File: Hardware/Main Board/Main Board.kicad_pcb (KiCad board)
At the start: 4 copper layers, 71 x 57.5 mm, 85 parts, among them J1 Micro_SD_Card_Det1, J3 Conn_01x09_Socket, J4 MIC 1 Connector, J5 MIC 2 Connector, J6 USB_C_Receptacle_USB2.0_16P, J7 OLED, Q1 AO3401A, SW1 SW_SPST, U1 ESP32-S3-WROOM-2, U2 TPS63060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

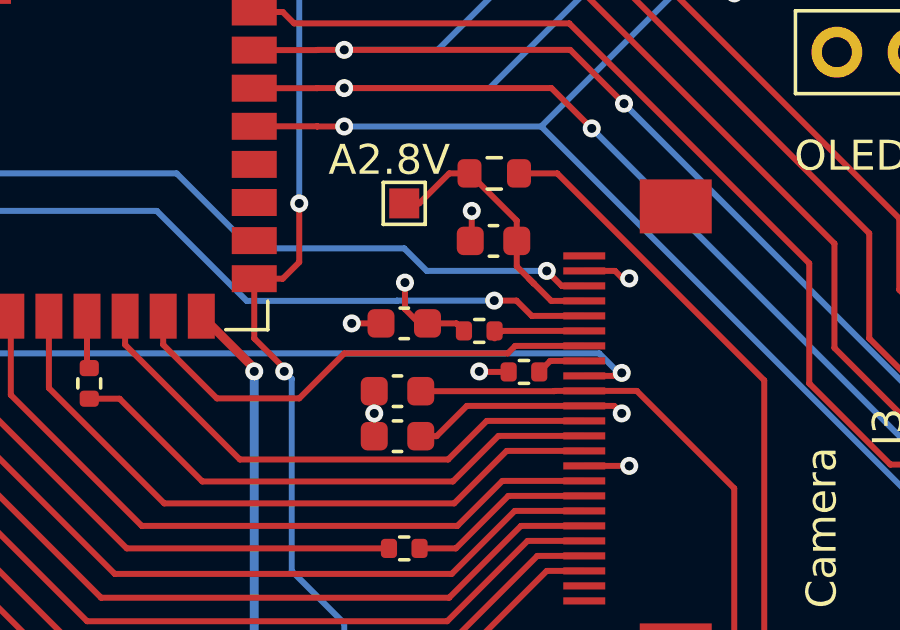
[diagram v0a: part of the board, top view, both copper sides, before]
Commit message: fixed drc issues
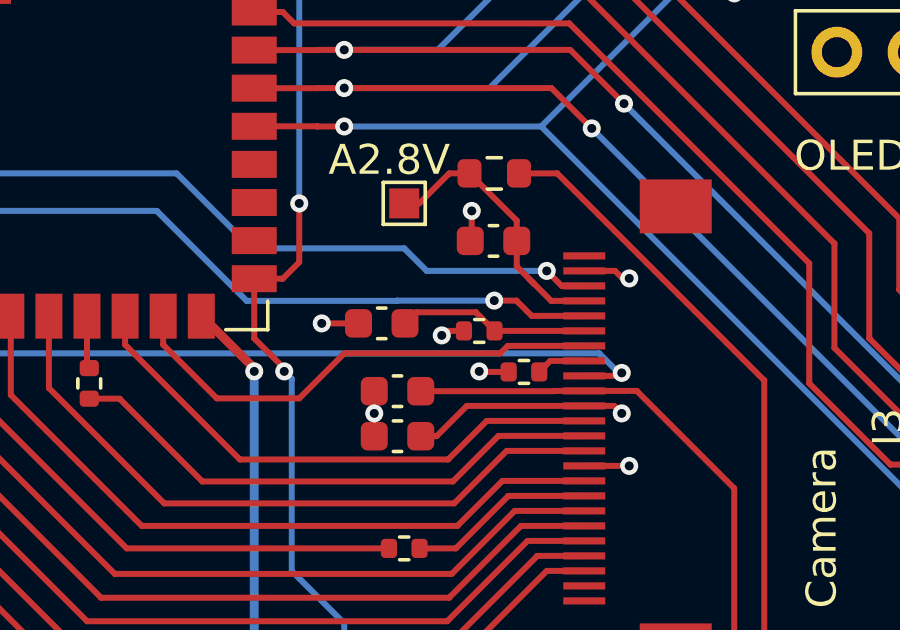
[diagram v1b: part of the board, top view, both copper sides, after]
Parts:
- moved C14 0.75 mm to (117.2, 68.0)
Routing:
- net Net-(CAM1-RESET): track 3.09 -> 6.39 mm
- net +3.3V: track 64.7 -> 62.2 mm
- net GND: track 72.7 -> 71.7 mm
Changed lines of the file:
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@@
 	(footprint "Capacitor_SMD:C_0603_1608Metric"
 		(layer "F.Cu")
-		(at 118 68 180)
+		(at 117.25 68 180)
 		(descr "Capacitor SMD 0603 (1608 Metric), square (rectangular) end terminal, IPC-7351 nominal, (Body size source: IPC-SM-782 page 76, https://www.pcb-3d.com/wordpress/wp-content/uploads/ipc-sm-782a_amendment_1_and_2.pdf), generated with kicad-footprint-generator")
 		(tags "capacitor")
@@
 	)
 	(gr_line
+		(start 115.25 68)
+		(end 116.5 68)
+		(stroke
+			(width 0.2)
+			(type default)
+		)
+		(layer "F.Cu")
+		(net 1)
+	)
+	(gr_line
 		(start 73.5 100)
 		(end 101 100)
@@
 	)
 	(segment
-		(start 116.25 68)
-		(end 117.225 68)
-		(width 0.2)
-		(layer "F.Cu")
-		(net 1)
-	)
-	(segment
 		(start 137.5 67)
 		(end 137.5 68.479888)
@@
 	)
 	(via
-		(at 116.25 68)
+		(at 115.25 68)
 		(size 0.6)
 		(drill 0.3)
@@
 	)
 	(segment
-		(start 118.5 68)
-		(end 118.775 68)
-		(width 0.2)
-		(layer "F.Cu")
-		(net 2)
-	)
-	(segment
 		(start 93.516996 51.151)
 		(end 95.381 51.151)
@@
 	)
 	(segment
-		(start 118.02392 66.64)
-		(end 118.02392 67.52392)
-		(width 0.2)
-		(layer "F.Cu")
-		(net 2)
-	)
-	(segment
-		(start 119.74 68)
-		(end 119.99 68.25)
-		(width 0.2)
-		(layer "F.Cu")
-		(net 2)
-	)
-	(segment
 		(start 125.05 82.524999)
 		(end 124.1 83.474999)
@@
 	)
 	(segment
+		(start 119.99 68.25)
+		(end 119.4 68.25)
+		(width 0.2)
+		(layer "F.Cu")
+		(net 2)
+	)
+	(segment
 		(start 92.399168 51.034004)
 		(end 92.399168 51.899168)
@@
 	)
 	(segment
-		(start 117.88392 66.5)
-		(end 118.02392 66.64)
-		(width 0.2)
-		(layer "F.Cu")
-		(net 2)
-	)
-	(segment
 		(start 77.016082 48.754598)
 		(end 77 48.738516)
@@
 	)
 	(segment
-		(start 118.02392 67.52392)
-		(end 118.5 68)
-		(width 0.2)
-		(layer "F.Cu")
-		(net 2)
-	)
-	(segment
 		(start 82.5 85.049904)
 		(end 82.5 85.5)
@@
 	)
 	(segment
+		(start 119.4 68.25)
+		(end 119.25 68.4)
+		(width 0.2)
+		(layer "F.Cu")
+		(net 2)
+	)
+	(segment
 		(start 78.094603 88.594603)
 		(end 78.321237 88.367968)
@@
 	)
 	(segment
-		(start 118.775 68)
-		(end 119.74 68)
-		(width 0.2)
-		(layer "F.Cu")
-		(net 2)
-	)
-	(segment
 		(start 85.5 86)
 		(end 84.946515 86.553485)
@@
 	)
 	(via
-		(at 118.02392 66.64)
-		(size 0.6)
-		(drill 0.3)
-		(layers "F.Cu" "B.Cu")
-		(net 2)
-	)
-	(via
 		(at 125.05 87.75)
 		(size 0.6)
@@
 	)
 	(via
+		(at 119.25 68.4)
+		(size 0.6)
+		(drill 0.3)
+		(layers "F.Cu" "B.Cu")
+		(net 2)
+	)
+	(via
 		(at 138.75 55)
 		(size 0.6)
@@
 	)
 	(segment
-		(start 121.70034 68.75)
-		(end 121.45034 69)
+		(start 111.755 70.5)
+		(end 109.965 68.71)
 		(width 0.2)
 		(layer "F.Cu")
@@
 	)
 	(segment
-		(start 111.755 70.5)
-		(end 109.965 68.71)
+		(start 124 68.75)
+		(end 121.45034 68.75)
 		(width 0.2)
 		(layer "F.Cu")
@@
 	)
 	(segment
-		(start 121.45034 69)
-		(end 116 69)
+		(start 114.5 70.5)
+		(end 111.755 70.5)
 		(width 0.2)
 		(layer "F.Cu")
@@
 	)
 	(segment
-		(start 114.5 70.5)
-		(end 111.755 70.5)
+		(start 116 69)
+		(end 114.5 70.5)
 		(width 0.2)
 		(layer "F.Cu")
@@
 	)
 	(segment
-		(start 116 69)
-		(end 114.5 70.5)
+		(start 121.20034 69)
+		(end 116 69)
 		(width 0.2)
 		(layer "F.Cu")
@@
 	)
 	(segment
-		(start 124 68.75)
-		(end 121.70034 68.75)
+		(start 121.45034 68.75)
+		(end 121.20034 69)
 		(width 0.2)
 		(layer "F.Cu")
@@
 	)
 	(segment
-		(start 121.26 68.25)
-		(end 124 68.25)
+		(start 124 68.25)
+		(end 121.01 68.25)
+		(width 0.2)
+		(layer "F.Cu")
+		(net 70)
+	)
+	(segment
+		(start 121.01 68.25)
+		(end 120.389 67.629)
+		(width 0.2)
+		(layer "F.Cu")
+		(net 70)
+	)
+	(segment
+		(start 120.389 67.629)
+		(end 118.396 67.629)
 		(width 0.2)
 		(layer "F.Cu")
@@
 	)
 	(segment
-		(start 121.01 68.5)
-		(end 121.26 68.25)
+		(start 118.396 67.629)
+		(end 118.025 68)
 		(width 0.2)
 		(layer "F.Cu")

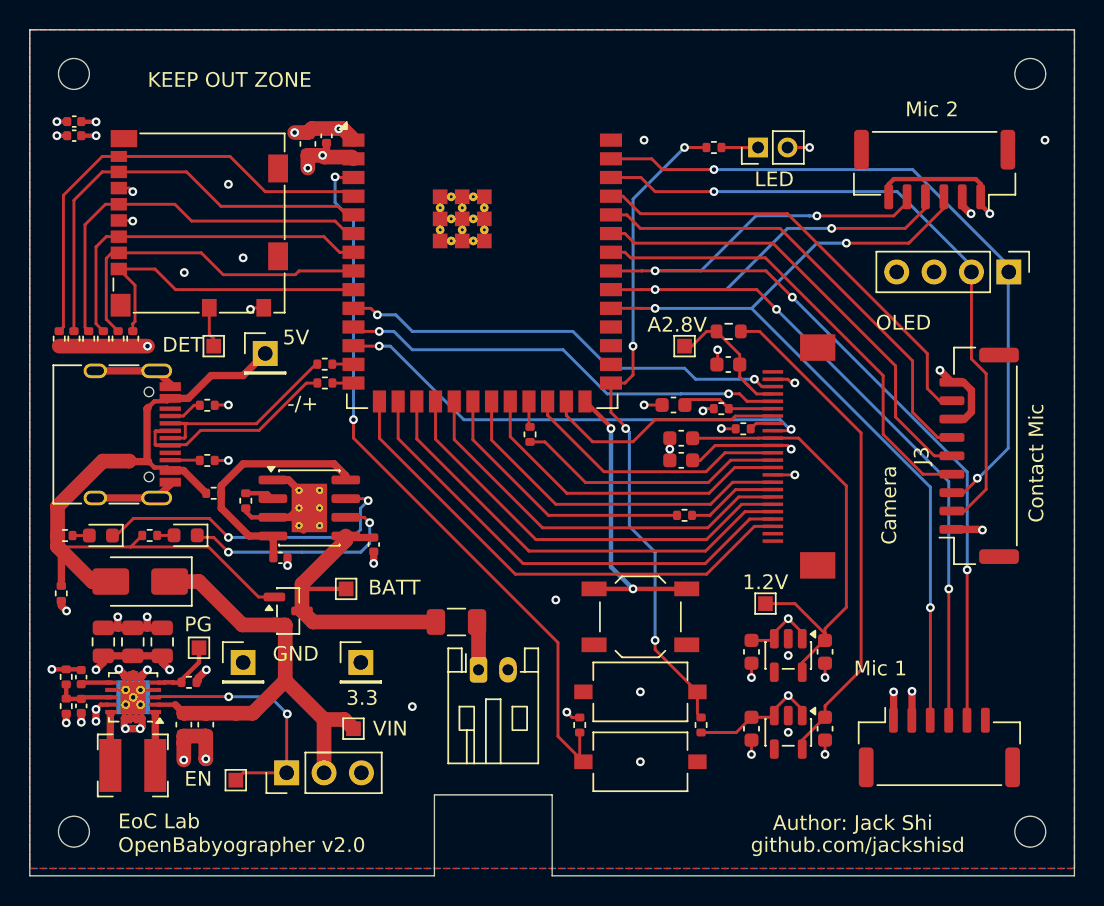
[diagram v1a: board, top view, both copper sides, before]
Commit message: Pull hardware updates from codex temp branch
Bring the main board hardware changes from origin/codex-temp-main-hardware-push onto main while excluding transient KiCad autosave and lock files.
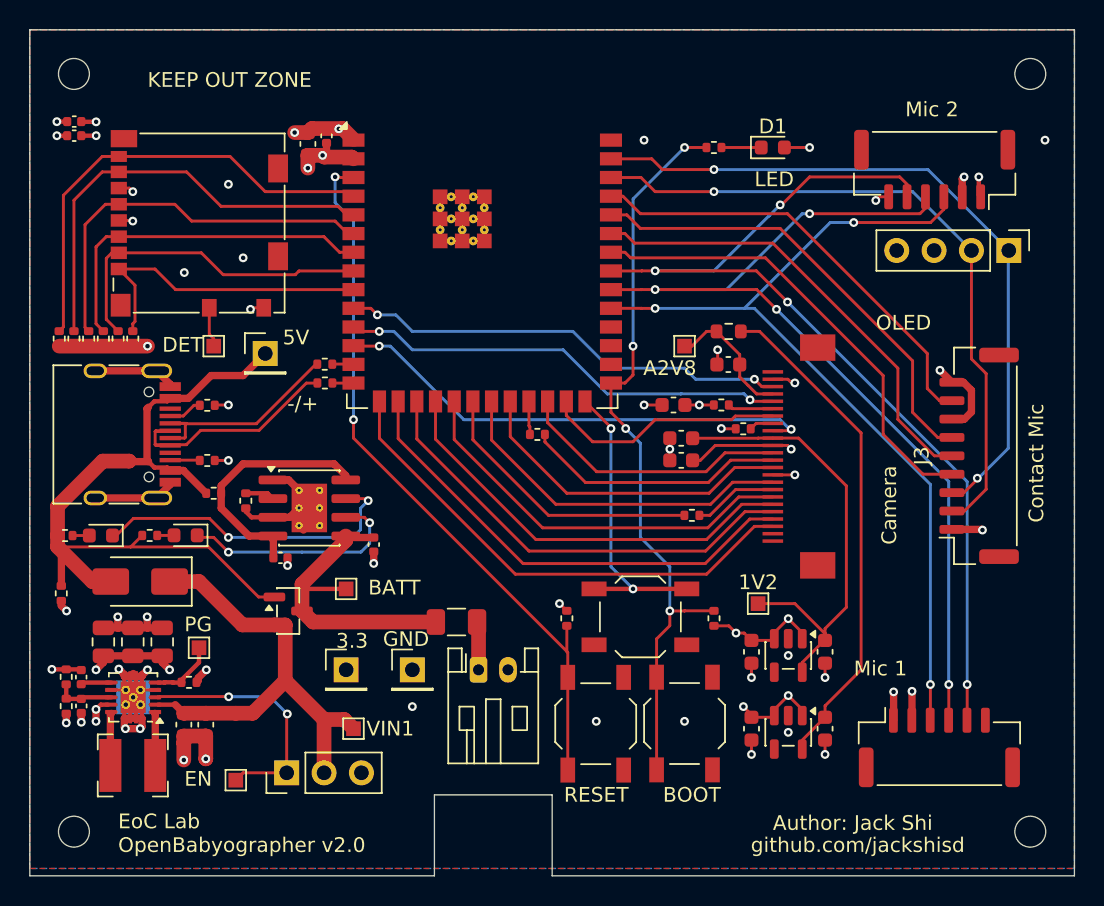
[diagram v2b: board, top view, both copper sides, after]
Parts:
- removed 1.2V, A2.8V, VIN: TestPoint, TestPoint:TestPoint_Pad_1.0x1.0mm
- removed BOOT1, RESET1: SW_Push, Button_Switch_SMD:SW_Tactile_SPST_NO_Straight_CK_PTS636Sx25SMTRLFS
- added 1V2: TestPoint, TestPoint:TestPoint_Pad_1.0x1.0mm, F.Cu at (123.0, 81.5)
- added A2V8: TestPoint, TestPoint:TestPoint_Pad_1.0x1.0mm, F.Cu at (118.0, 64.0)
- added BOOT: SW_Push, Button_Switch_SMD:SW_SPST_TL3342, F.Cu at (118.0, 89.7)
- added RESET: SW_Push, Button_Switch_SMD:SW_SPST_TL3342, F.Cu at (112.0, 89.7)
- added VIN1: TestPoint, TestPoint:TestPoint_Pad_1.0x1.0mm, F.Cu at (95.5, 90.0)
- D1: footprint Connector_PinHeader_2.00mm:PinHeader_1x02_P2.00mm_Vertical -> LED_SMD:LED_0603_1608Metric
- R13, R14: value 1k -> 4.7k
- R15: value 0.4 -> 0
- moved TP1 11.5 mm to (99.5, 86.0)
- moved R1 7.30 mm to (110.0, 82.5)
- moved R12 7.30 mm to (120.0, 82.5)
- moved J7 1.46 mm to (140.0, 57.5)
- moved TP2 1.12 mm to (95.0, 86.0)
- moved D1 1.00 mm to (124.0, 50.5), turned to 0 degrees
- moved R23 0.50 mm to (108.0, 70.0), turned to 0 degrees
- moved R28 0.50 mm to (118.5, 75.5)
- moved R26 0.25 mm to (120.5, 68.0)
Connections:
- C14 pad 1: Net-(CAM1-RESET) -> +3.3V
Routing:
- net Net-(U1-IO0): track 45.0 -> 51.5 mm
- net +3.3V: track 62.2 -> 55.8 mm, vias 21 -> 24
- net Net-(CAM1-RESET): track 6.39 -> 3.09 mm
- net MIC_LCRL: track 66.2 -> 67.6 mm
- net I2C_SDA: track 47.7 -> 48.9 mm
- net MIC_BCLK: track 59.2 -> 59.9 mm
- net Net-(U1-IO21): track 1.66 -> 2.27 mm
- net I2C_SCL: track 45.1 -> 45.6 mm
- net Net-(U1-IO12): track 18.6 -> 19.1 mm
- net CAM_XCLK: track 18.3 -> 17.8 mm
- net CAM_PCLK: track 6.21 -> 5.71 mm
- net GND: vias 45 -> 44

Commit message: submitted for manufacturing
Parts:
- removed BOOT, RESET: SW_Push, Button_Switch_SMD:SW_SPST_TL3342
- removed TP1, TP2: TestPoint, Connector_PinHeader_2.54mm:PinHeader_1x01_P2.54mm_Vertical
- removed TP5: TestPoint, TestPoint:TestPoint_Pad_1.0x1.0mm
- added 3V3: TestPoint, Connector_PinHeader_2.54mm:PinHeader_1x01_P2.54mm_Vertical, F.Cu at (95.0, 86.0)
- added BATT1: TestPoint, TestPoint:TestPoint_Pad_1.0x1.0mm, F.Cu at (95.0, 80.5)
- added BOOT1: SW_Push, Button_Switch_SMD:SW_SPST_TL3342, F.Cu at (118.0, 89.7)
- added GND1: TestPoint, Connector_PinHeader_2.54mm:PinHeader_1x01_P2.54mm_Vertical, F.Cu at (99.5, 86.0)
- added RESET1: SW_Push, Button_Switch_SMD:SW_SPST_TL3342, F.Cu at (112.0, 89.7)
- D1: footprint LED_SMD:LED_0603_1608Metric -> Connector_PinHeader_2.54mm:PinHeader_1x02_P2.54mm_Vertical
- R11: value 10k -> 4.7k
- R13, R14: value 4.7k -> 10k
- moved 600Ω@100MHz1 25.1 mm to (123.0, 88.0)
- moved A2V8 2.00 mm to (120.0, 64.0)
- moved C16 1.25 mm to (121.0, 66.5)
- moved J7 1.04 mm to (139.0, 57.5)
- moved D1 0.99 mm to (123.0, 50.5), turned to 90 degrees
- moved C20 0.73 mm to (122.6, 90.7)
- moved C21 0.73 mm to (127.6, 90.7)
- moved U4 0.73 mm to (125.1, 91.0)
- moved TP7 0.50 mm to (87.5, 93.0)
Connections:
- 600Ω@100MHz1 pad 1: Net-(U4-OUT) -> +3.3V
- 600Ω@100MHz1 pad 2: 2.8V -> Net-(U4-IN)
- C20 pad 1: +3.3V -> Net-(U4-IN)
- C21 pad 1: Net-(U4-OUT) -> 2.8V
- U4 pad 1: +3.3V -> Net-(U4-IN)
- U4 pad 5: Net-(U4-OUT) -> 2.8V
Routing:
- net Net-(U4-OUT): track 33.6 -> 0.00 mm
- net 2.8V: track 9.07 -> 35.8 mm
- net Net-(U4-IN): track 0.00 -> 8.64 mm
- net +3.3V: track 55.8 -> 54.8 mm, vias 24 -> 23
- net I2C_SDA: track 48.9 -> 48.1 mm
- net I2C_SCL: track 45.6 -> 46.3 mm
- net GND: track 71.7 -> 71.5 mm, vias 44 -> 46
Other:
- board text removed: "3.3"
- board text removed: "BATT"
- board text removed: "GND"
